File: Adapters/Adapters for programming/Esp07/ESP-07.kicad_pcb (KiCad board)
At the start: 2 copper layers, 4 parts, among them U1 ESP-07

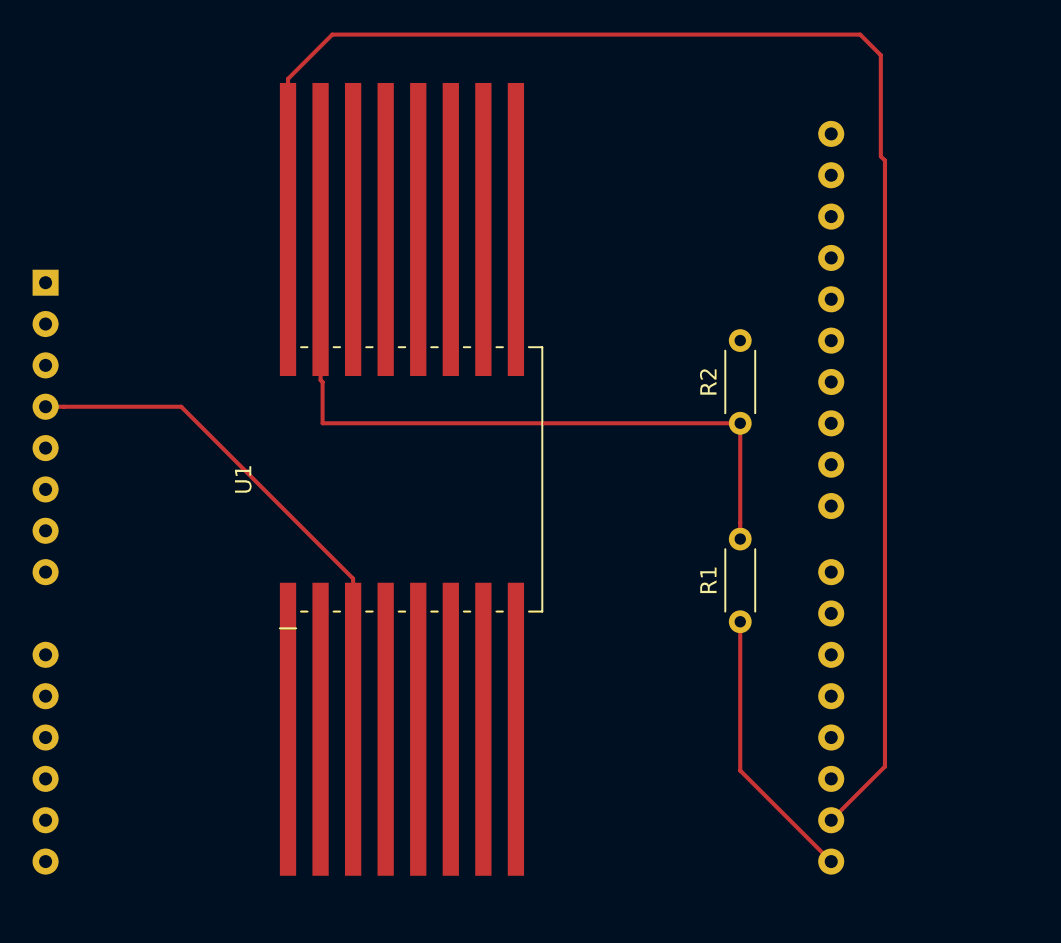
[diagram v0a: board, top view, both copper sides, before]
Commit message: Fixed error in ESP breadboard adapter footprint, updated the schema to wire the for the new layout. Updated the ESP flashing adapter.
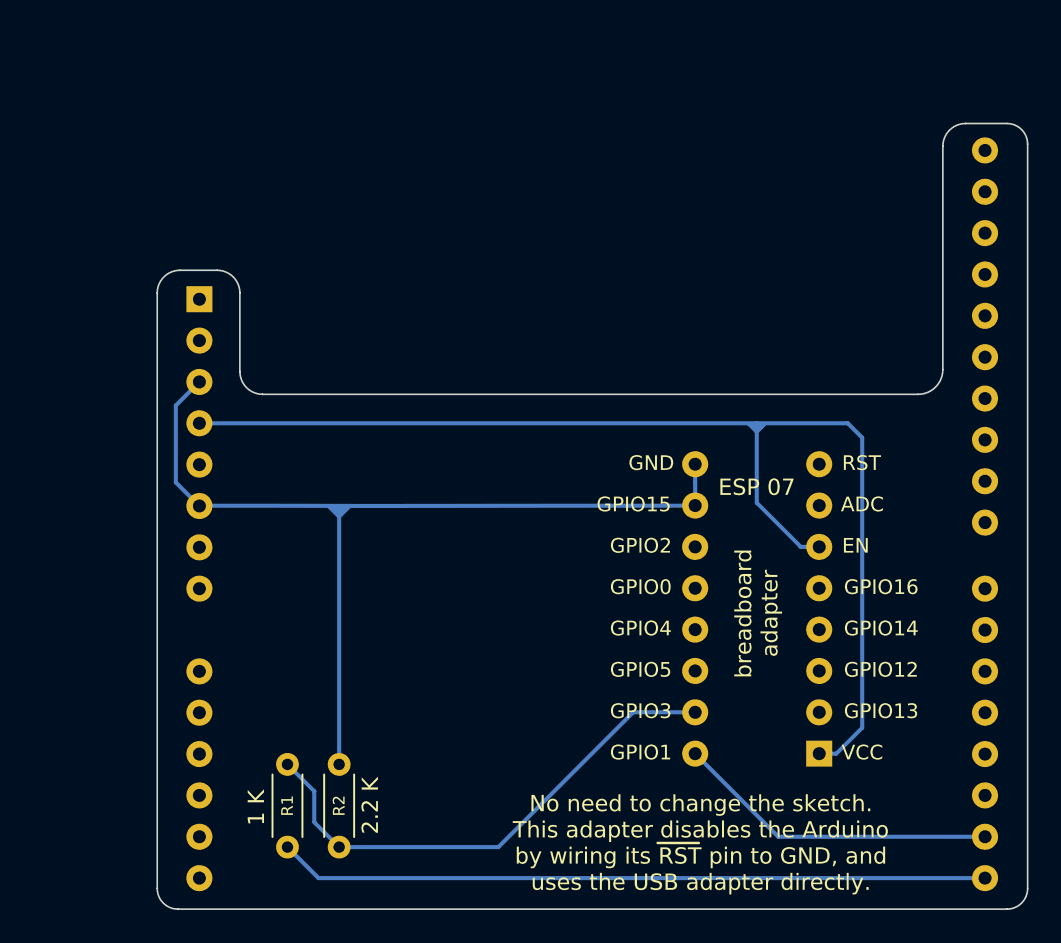
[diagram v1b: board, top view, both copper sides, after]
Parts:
- A1: footprint ArduinoUnoMultiProgrammerAdapters:Arduino-UNO-R3-Shield -> ArduinoUnoMultiProgrammerAdapters:Arduino_UNO_R3_Headers; moved to F.Cu
- U1: footprint ArduinoUnoMultiProgrammerAdapters:ESP-07-Socket -> ArduinoUnoMultiProgrammerAdapters:ESP07BreaboardSocket
- moved R2 35.8 mm to (146.1, 118.7)
- moved A1 32.7 mm to (160.3, 89.5), turned to 0 degrees
- moved R1 31.1 mm to (142.9, 118.7)
- moved U1 24.8 mm to (171.7, 102.6), turned to 0 degrees
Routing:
- net Net-(A1-Pad16): track 95.8 -> 19.9 mm
- net GND: track 0.00 -> 57.7 mm
- net Net-(A1-Pad4): track 32.5 -> 72.0 mm
- net Net-(A1-Pad15): track 17.0 -> 43.6 mm
- net Net-(R1-Pad2): track 44.7 -> 31.7 mm
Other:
- board outline added: 53.5 x 48.3 mm
- board text added: "ESP 07"
- board text added: "No need to change the sketch. This adapter disables the Arduino by wiring its RST pin to GND, and uses the USB adapter directly."
- board text added: "breadboard adapter"

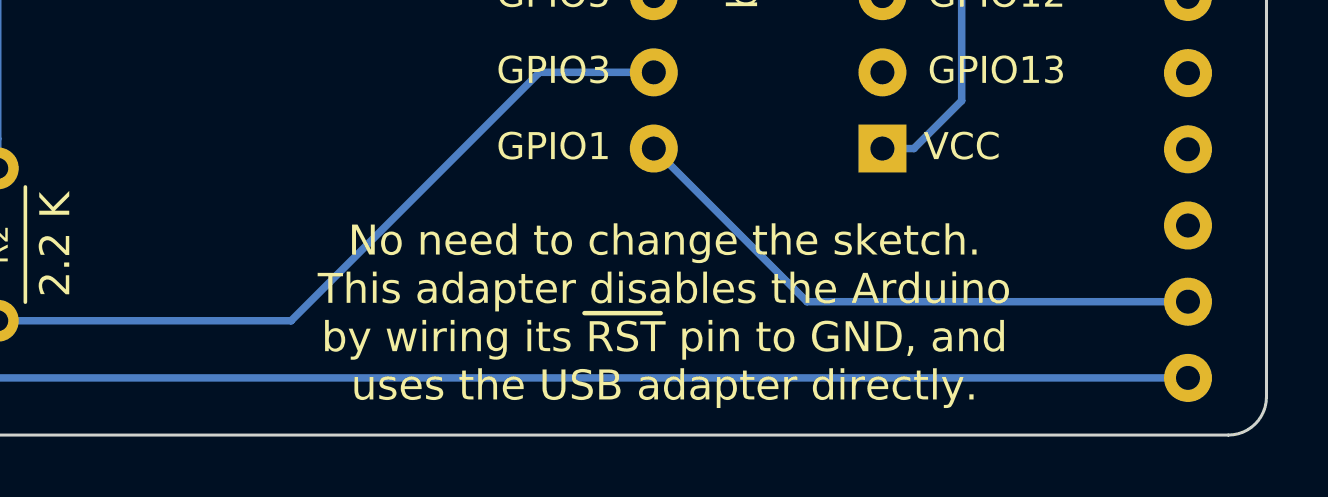
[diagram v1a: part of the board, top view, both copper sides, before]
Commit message: Signed all the boards, and re-generated the Gerber files
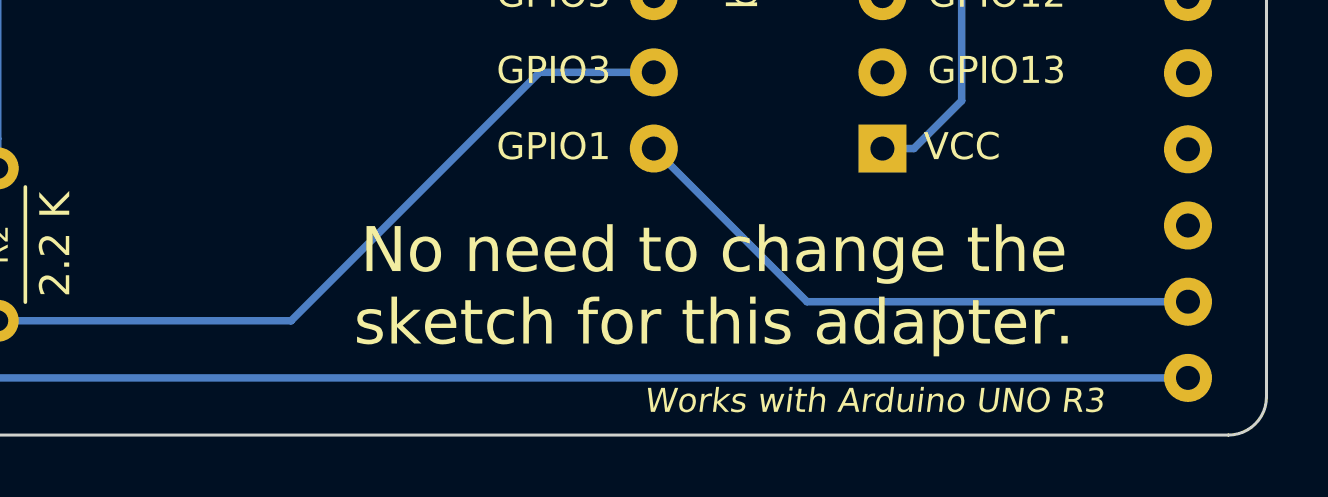
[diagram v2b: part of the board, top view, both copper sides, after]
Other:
- board text added: "March 2020"
- board text added: "No need to change the sketch for this adapter."
- board text added: "Works with Arduino UNO R3"
- board text added: "by Razvan"
- board text removed: "No need to change the sketch. This adapter disables the Arduino by wiring its RST pin to GND, and uses the USB adapter directly."
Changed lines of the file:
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@@
   (general
     (thickness 1.6)
-    (drawings 22)
+    (drawings 25)
     (tracks 29)
     (zones 0)
@@
   (layers
     (0 F.Cu signal)
-    (31 B.Cu signal hide)
+    (31 B.Cu signal)
     (32 B.Adhes user)
     (33 F.Adhes user)
@@
     (uvia_drill 0.1)
     (add_net GND)
-    (add_net "Net-(A1-Pad1)")
-    (add_net "Net-(A1-Pad10)")
-    (add_net "Net-(A1-Pad11)")
-    (add_net "Net-(A1-Pad12)")
-    (add_net "Net-(A1-Pad13)")
-    (add_net "Net-(A1-Pad14)")
     (add_net "Net-(A1-Pad15)")
     (add_net "Net-(A1-Pad16)")
-    (add_net "Net-(A1-Pad17)")
-    (add_net "Net-(A1-Pad18)")
-    (add_net "Net-(A1-Pad19)")
-    (add_net "Net-(A1-Pad2)")
-    (add_net "Net-(A1-Pad20)")
-    (add_net "Net-(A1-Pad21)")
-    (add_net "Net-(A1-Pad22)")
-    (add_net "Net-(A1-Pad23)")
-    (add_net "Net-(A1-Pad24)")
-    (add_net "Net-(A1-Pad25)")
-    (add_net "Net-(A1-Pad26)")
-    (add_net "Net-(A1-Pad27)")
-    (add_net "Net-(A1-Pad28)")
-    (add_net "Net-(A1-Pad29)")
-    (add_net "Net-(A1-Pad30)")
-    (add_net "Net-(A1-Pad31)")
-    (add_net "Net-(A1-Pad32)")
     (add_net "Net-(A1-Pad4)")
-    (add_net "Net-(A1-Pad5)")
-    (add_net "Net-(A1-Pad7)")
-    (add_net "Net-(A1-Pad8)")
-    (add_net "Net-(A1-Pad9)")
     (add_net "Net-(R1-Pad2)")
-    (add_net "Net-(U1-Pad1)")
-    (add_net "Net-(U1-Pad11)")
-    (add_net "Net-(U1-Pad12)")
-    (add_net "Net-(U1-Pad13)")
-    (add_net "Net-(U1-Pad14)")
-    (add_net "Net-(U1-Pad2)")
-    (add_net "Net-(U1-Pad4)")
-    (add_net "Net-(U1-Pad5)")
-    (add_net "Net-(U1-Pad6)")
-    (add_net "Net-(U1-Pad7)")
   )
   (module ArduinoUnoMultiProgrammerAdapters:ESP07BreaboardSocket (layer F.Cu)
@@
     )
   )
-  (gr_line (start 165.608 118.491) (end 168.148 118.491) (layer F.SilkS) (width 0.15))
-  (gr_text "No need to change the sketch.\nThis adapter disables the Arduino\nby wiring its RST pin to GND, and\nuses the USB adapter directly." (at 168.275 118.491) (layer F.SilkS)
-    (effects (font (size 1 1) (thickness 0.15)))
+  (gr_text "Works with Arduino UNO R3" (at 175.26 121.412) (layer F.SilkS)
+    (effects (font (size 0.8 0.8) (thickness 0.15) italic))
+  )
+  (gr_arc (start 145.669 93.599) (end 145.415 93.726) (angle -126.9) (layer B.SilkS) (width 0.2))
+  (gr_text "March 2020" (at 144.399 96.393) (layer B.SilkS)
+    (effects (font (size 1 1) (thickness 0.15)) (justify mirror))
+  )
+  (gr_text "by Razvan" (at 145.669 94.615) (layer B.SilkS)
+    (effects (font (size 1.5 1.5) (thickness 0.3)) (justify mirror))
+  )
+  (gr_text "No need to change the \nsketch for this adapter." (at 169.926 117.602) (layer F.SilkS)
+    (effects (font (size 1.5 1.5) (thickness 0.15)))
   )
   (gr_poly (pts (xy 146.05 98.552) (xy 145.288 97.79) (xy 146.812 97.79)) (layer B.Cu) (width 0.1))

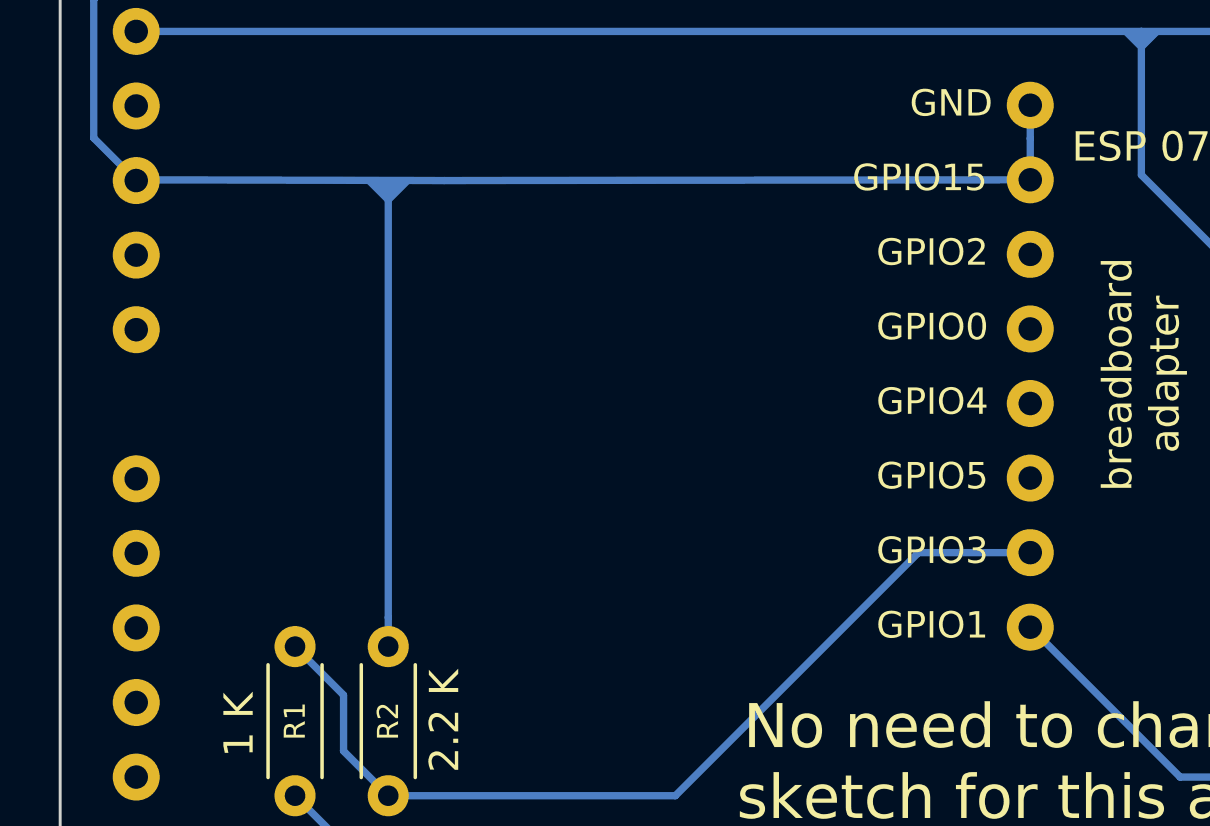
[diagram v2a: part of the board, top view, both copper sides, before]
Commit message: Fixed schematic for ESP adapter and regenerated Gerber files
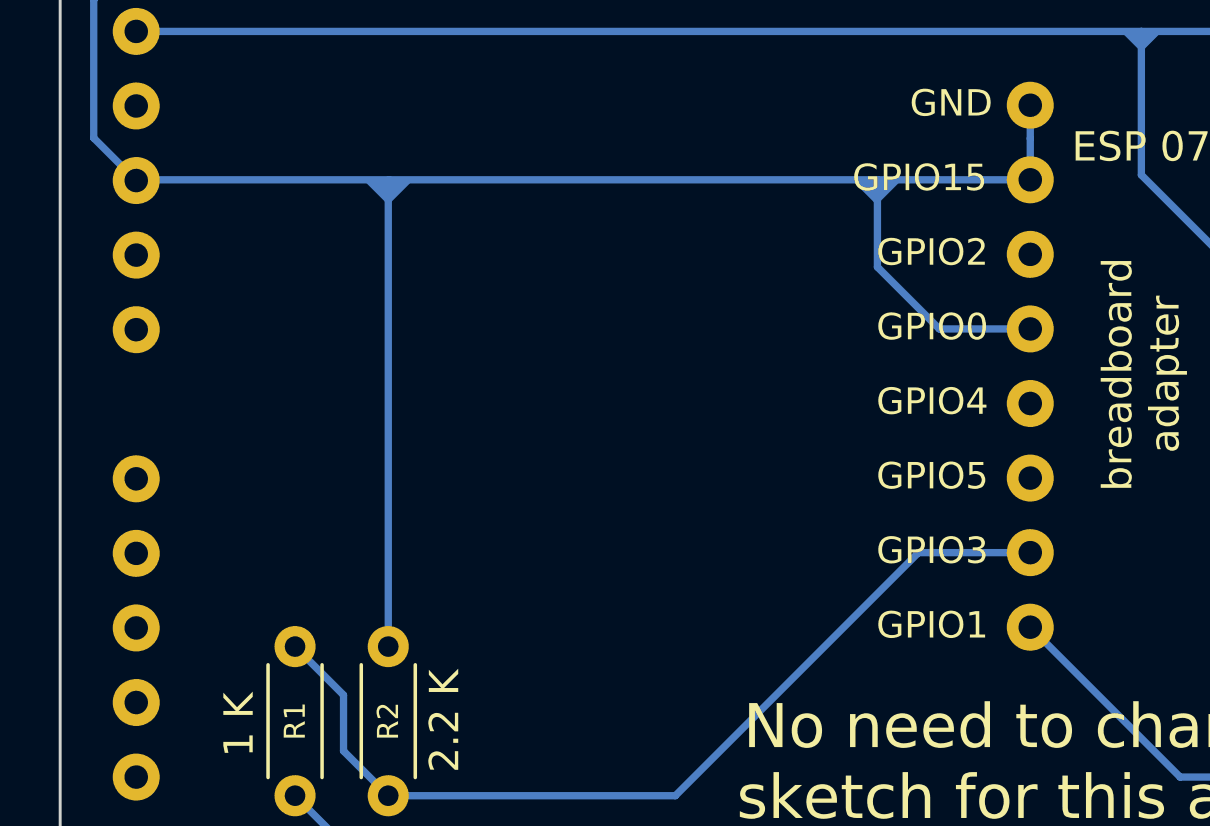
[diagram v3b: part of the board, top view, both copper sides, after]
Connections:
- U1 pad 12: (no net) -> GND
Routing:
- net GND: track 57.7 -> 66.8 mm
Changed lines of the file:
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@@
   (general
     (thickness 1.6)
-    (drawings 25)
-    (tracks 29)
+    (drawings 26)
+    (tracks 33)
     (zones 0)
     (modules 4)
@@
     (pad 13 thru_hole oval (at -3.7846 2.7686 180) (size 1.6 1.6) (drill 0.8) (layers *.Cu *.Mask))
     (pad 4 thru_hole oval (at 3.8354 0.2286 180) (size 1.6 1.6) (drill 0.8) (layers *.Cu *.Mask))
-    (pad 12 thru_hole oval (at -3.7846 0.2286 180) (size 1.6 1.6) (drill 0.8) (layers *.Cu *.Mask))
+    (pad 12 thru_hole oval (at -3.7846 0.2286 180) (size 1.6 1.6) (drill 0.8) (layers *.Cu *.Mask)
+      (net 3 GND))
     (pad 5 thru_hole oval (at 3.8354 2.7686 180) (size 1.6 1.6) (drill 0.8) (layers *.Cu *.Mask))
     (pad 11 thru_hole oval (at -3.7846 -2.3114 180) (size 1.6 1.6) (drill 0.8) (layers *.Cu *.Mask))
@@
     )
   )
+  (gr_poly (pts (xy 162.687 98.552) (xy 161.925 97.79) (xy 163.449 97.79)) (layer B.Cu) (width 0.1))
   (gr_text "Works with Arduino UNO R3" (at 175.26 121.412) (layer F.SilkS)
     (effects (font (size 0.8 0.8) (thickness 0.15) italic))
@@
   (segment (start 167.9194 95.2246) (end 167.9194 96.35597) (width 0.25) (layer B.Cu) (net 3))
   (segment (start 137.4902 97.7646) (end 137.4648 97.79) (width 0.25) (layer B.Cu) (net 3))
-  (segment (start 146.05 112.675051) (end 146.05 97.79) (width 0.25) (layer B.Cu) (net 3))
-  (segment (start 146.05 113.665) (end 146.05 112.675051) (width 0.25) (layer B.Cu) (net 3))
-  (segment (start 167.9194 97.7646) (end 147.955 97.79) (width 0.25) (layer B.Cu) (net 3))
-  (segment (start 147.955 97.79) (end 137.4902 97.7646) (width 0.25) (layer B.Cu) (net 3))
+  (segment (start 167.9194 102.8446) (end 164.8206 102.8446) (width 0.25) (layer B.Cu) (net 3))
+  (segment (start 162.7124 100.7364) (end 162.7124 97.7646) (width 0.25) (layer B.Cu) (net 3))
+  (segment (start 164.8206 102.8446) (end 162.7124 100.7364) (width 0.25) (layer B.Cu) (net 3))
+  (segment (start 167.9194 97.7646) (end 162.7124 97.7646) (width 0.25) (layer B.Cu) (net 3))
+  (segment (start 146.05 97.79) (end 146.0754 97.7646) (width 0.25) (layer B.Cu) (net 3))
+  (segment (start 146.05 113.665) (end 146.05 97.79) (width 0.25) (layer B.Cu) (net 3))
+  (segment (start 162.7124 97.7646) (end 146.0754 97.7646) (width 0.25) (layer B.Cu) (net 3))
+  (segment (start 146.0754 97.7646) (end 137.4902 97.7646) (width 0.25) (layer B.Cu) (net 3))
   (segment (start 176.5894 113.0046) (end 178.181 111.413) (width 0.25) (layer B.Cu) (net 4))
   (segment (start 175.5394 113.0046) (end 176.5894 113.0046) (width 0.25) (layer B.Cu) (net 4))
